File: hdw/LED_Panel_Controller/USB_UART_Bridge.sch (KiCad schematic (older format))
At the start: 37 parts, among them J1501 USB_B_Mini, U1501 TLV6700, U1502 FT234XD, U1503 TXB0102DCU, U1504 TPD3S014DBVR

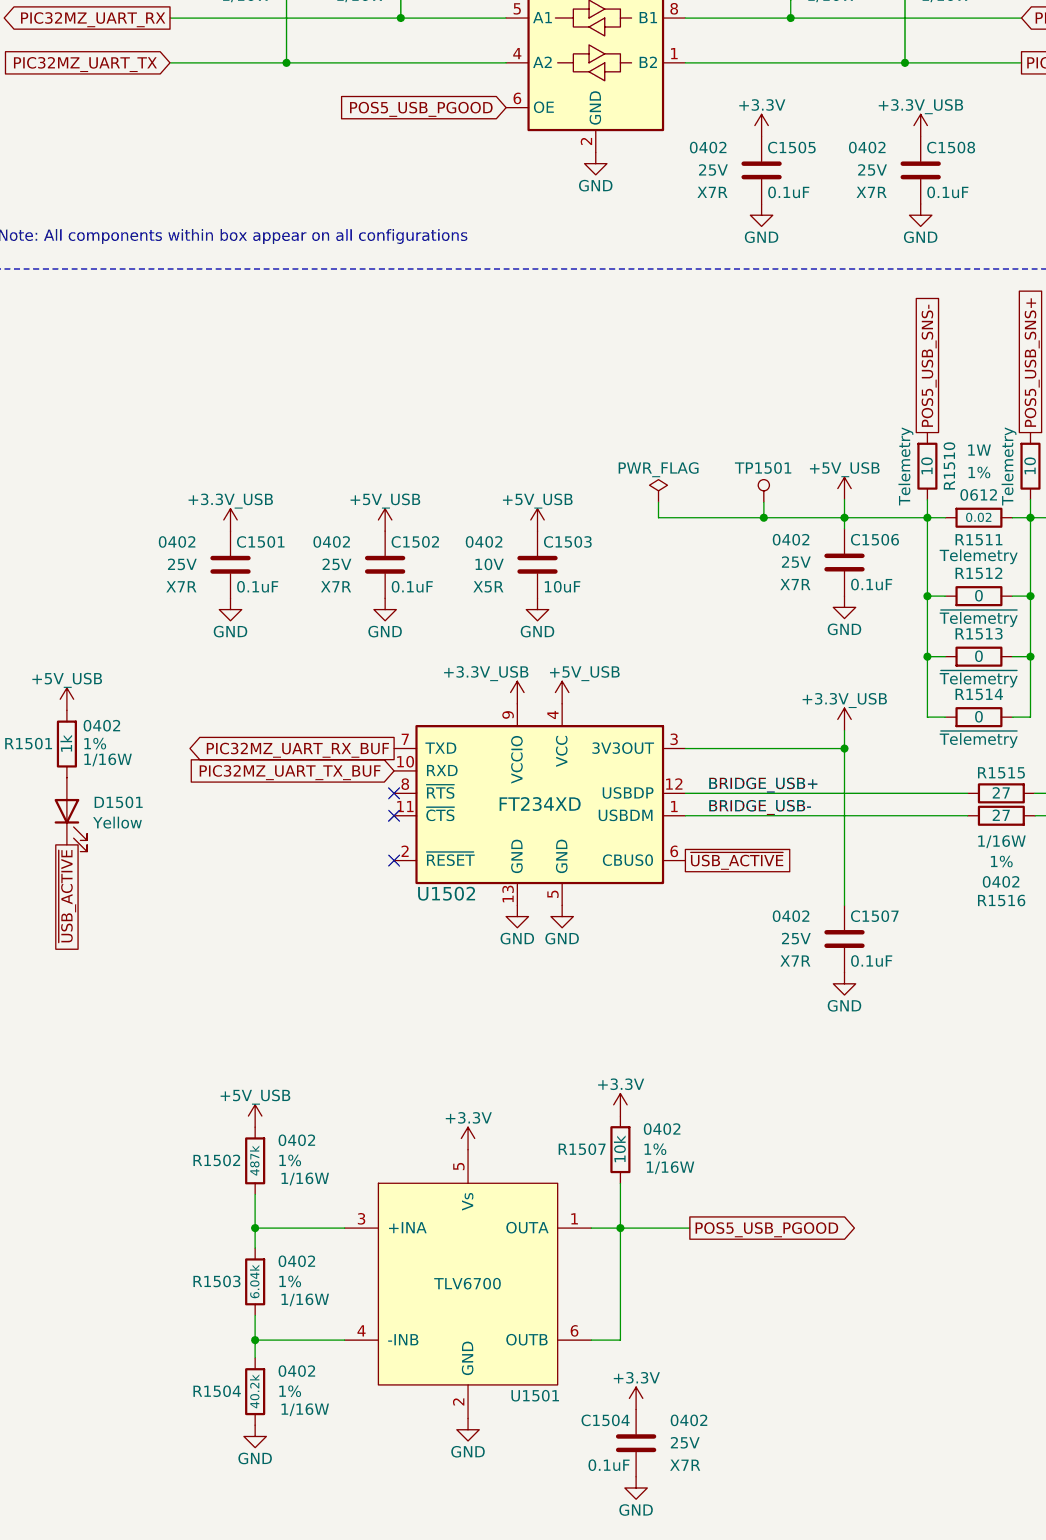
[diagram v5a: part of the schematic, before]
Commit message: added BOMs, some consolidation
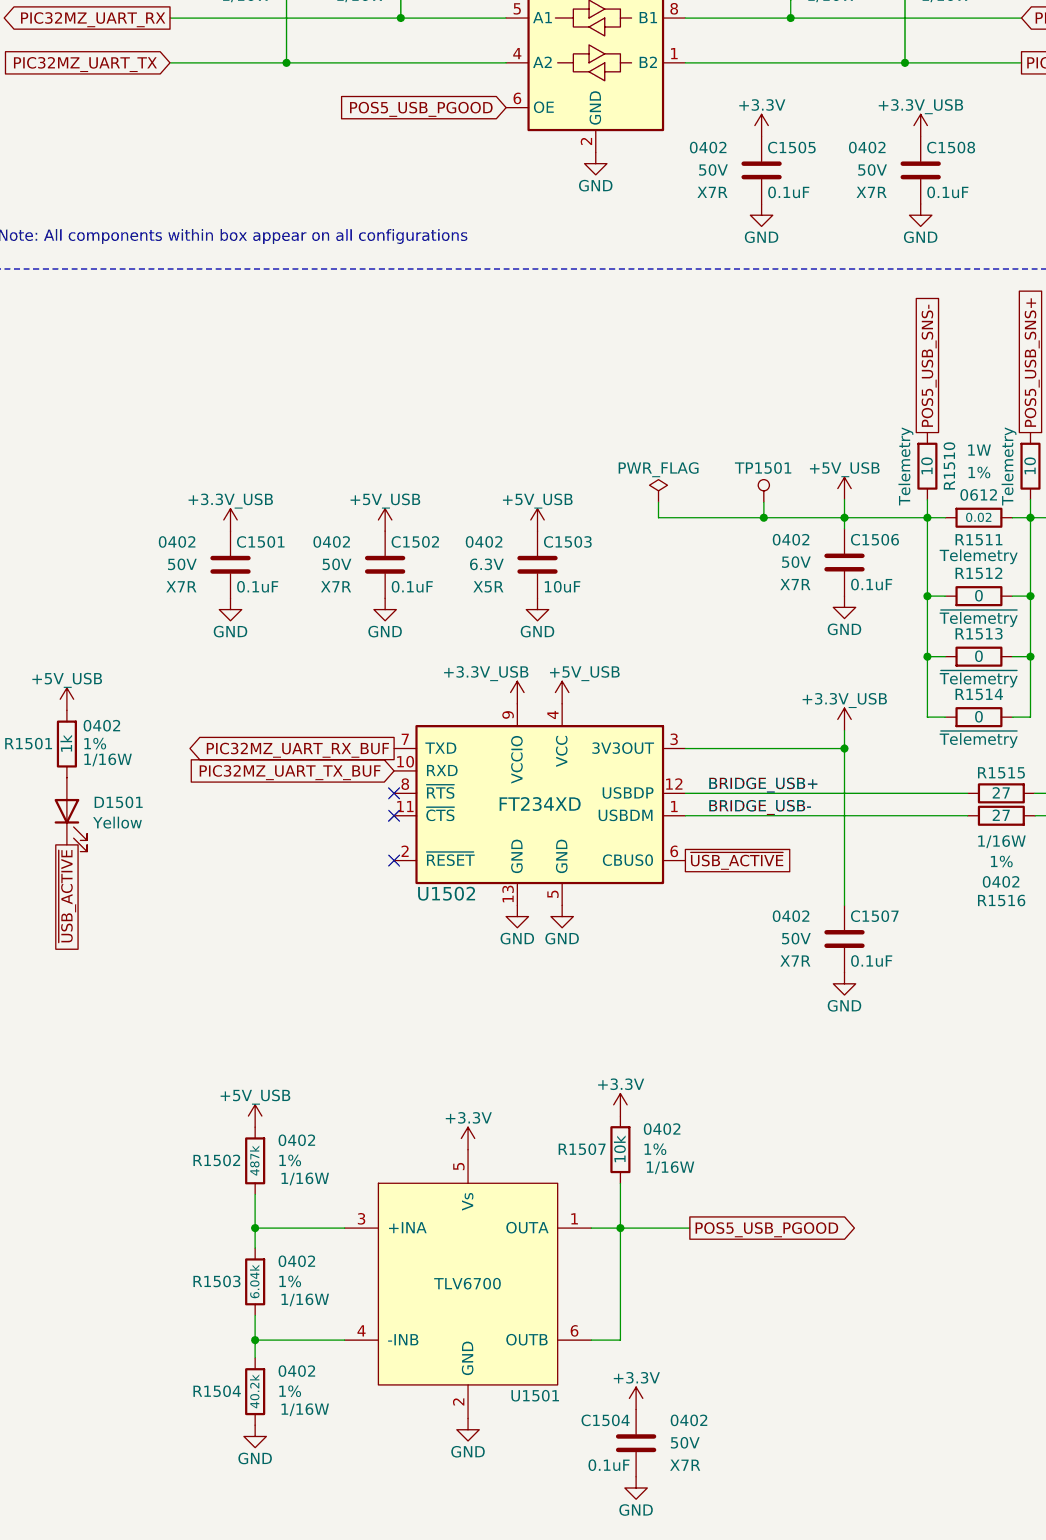
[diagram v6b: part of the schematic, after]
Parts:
- C1203: Digi-Key PN 1276-6830-1-ND -> 1276-1451-1-ND; Voltage 10V -> 6.3V
- C1204, C1501, C1502, C1505, C1506, C1507, C1508: Voltage 25V -> 50V
- R1210, R1211, R1212: Digi-Key PN 2019-RK73Z1ETTPCT-ND -> RMCF0402ZT0R00CT-N
- R1504: Digi-Key PN 311-40.2KLRCT-ND -> RMCF0402FT40K2CT-ND
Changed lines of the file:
@@
 F 3 "" H 2385 3780 50  0001 C CNN
 F 4 "0402" H 2210 3780 50  0000 R CNN "display_footprint"
-F 5 "25V" H 2210 3680 50  0000 R CNN "Voltage"
+F 5 "50V" H 2210 3680 50  0000 R CNN "Voltage"
 F 6 "X7R" H 2210 3580 50  0000 R CNN "Dielectric"
 F 7 "490-10698-1-ND" H 2785 4180 60  0001 C CNN "Digi-Key PN"
@@
 F 3 "" H 1695 3780 50  0001 C CNN
 F 4 "0402" H 1520 3780 50  0000 R CNN "display_footprint"
-F 5 "25V" H 1520 3680 50  0000 R CNN "Voltage"
+F 5 "50V" H 1520 3680 50  0000 R CNN "Voltage"
 F 6 "X7R" H 1520 3580 50  0000 R CNN "Dielectric"
 F 7 "490-10698-1-ND" H 2095 4180 60  0001 C CNN "Digi-Key PN"
@@
 F 3 "" H 4435 5450 50  0001 C CNN
 F 4 "0402" H 4260 5450 50  0000 R CNN "display_footprint"
-F 5 "25V" H 4260 5350 50  0000 R CNN "Voltage"
+F 5 "50V" H 4260 5350 50  0000 R CNN "Voltage"
 F 6 "X7R" H 4260 5250 50  0000 R CNN "Dielectric"
 F 7 "490-10698-1-ND" H 4835 5850 60  0001 C CNN "Digi-Key PN"
@@
 F 5 "1%" H 1880 7370 50  0000 L CNN "Tolerance"
 F 6 "1/16W" H 1890 7290 50  0000 L CNN "Wattage"
-F 7 "311-40.2KLRCT-ND" H 2080 7770 60  0001 C CNN "Digi-Key PN"
+F 7 "RMCF0402FT40K2CT-ND" H 2080 7770 60  0001 C CNN "Digi-Key PN"
 F 8 "USB" H 1780 7370 50  0001 C CNN "Configuration"
 	1    1780 7370
@@
 F 4 "490-10698-1-ND" H 3905 8100 60  0001 C CNN "Digi-Key PN"
 F 5 "0402" H 3330 7700 50  0000 R CNN "display_footprint"
-F 6 "25V" H 3330 7600 50  0000 R CNN "Voltage"
+F 6 "50V" H 3330 7600 50  0000 R CNN "Voltage"
 F 7 "X7R" H 3330 7500 50  0000 R CNN "Dielectric"
 F 8 "USB" H 3480 7600 50  0001 C CNN "Configuration"
@@
 F 3 "" H 4435 3770 50  0001 C CNN
 F 4 "0402" H 4260 3770 50  0000 R CNN "display_footprint"
-F 5 "25V" H 4260 3670 50  0000 R CNN "Voltage"
+F 5 "50V" H 4260 3670 50  0000 R CNN "Voltage"
 F 6 "X7R" H 4260 3570 50  0000 R CNN "Dielectric"
 F 7 "490-10698-1-ND" H 4835 4170 60  0001 C CNN "Digi-Key PN"
@@
 F 3 "" H 4065 2020 50  0001 C CNN
 F 4 "0402" H 3890 2020 50  0000 R CNN "display_footprint"
-F 5 "25V" H 3890 1920 50  0000 R CNN "Voltage"
+F 5 "50V" H 3890 1920 50  0000 R CNN "Voltage"
 F 6 "X7R" H 3890 1820 50  0000 R CNN "Dielectric"
 F 7 "490-10698-1-ND" H 4040 1920 50  0001 C CNN "Digi-Key PN"
@@
 F 3 "" H 4775 2020 50  0001 C CNN
 F 4 "0402" H 4600 2020 50  0000 R CNN "display_footprint"
-F 5 "25V" H 4600 1920 50  0000 R CNN "Voltage"
+F 5 "50V" H 4600 1920 50  0000 R CNN "Voltage"
 F 6 "X7R" H 4600 1820 50  0000 R CNN "Dielectric"
 F 7 "490-10698-1-ND" H 4750 1920 50  0001 C CNN "Digi-Key PN"
@@
 F 3 "" H 3065 3780 50  0001 C CNN
 F 4 "0402" H 2890 3780 50  0000 R CNN "display_footprint"
-F 5 "10V" H 2890 3680 50  0000 R CNN "Voltage"
+F 5 "6.3V" H 2890 3680 50  0000 R CNN "Voltage"
 F 6 "X5R" H 2890 3580 50  0000 R CNN "Dielectric"
-F 7 "1276-6830-1-ND" H 3040 3680 50  0001 C CNN "Digi-Key PN"
+F 7 "1276-1451-1-ND" H 3040 3680 50  0001 C CNN "Digi-Key PN"
 F 8 "USB" H 3040 3680 50  0001 C CNN "Configuration"
 	1    3040 3680
@@
 F 6 "1/16W" V 5310 3820 50  0001 C CNN "Wattage"
 F 7 "~Telemetry" V 5110 3820 50  0000 C CNN "Configuration"
-F 8 "2019-RK73Z1ETTPCT-ND" H 5010 3820 50  0001 C CNN "Digi-Key PN"
+F 8 "RMCF0402ZT0R00CT-N" H 5010 3820 50  0001 C CNN "Digi-Key PN"
 	1    5010 3820
 	0    -1   1    0
@@
 F 6 "1/16W" V 5310 4090 50  0001 C CNN "Wattage"
 F 7 "~Telemetry" V 5110 4090 50  0000 C CNN "Configuration"
-F 8 "2019-RK73Z1ETTPCT-ND" H 5010 4090 50  0001 C CNN "Digi-Key PN"
+F 8 "RMCF0402ZT0R00CT-N" H 5010 4090 50  0001 C CNN "Digi-Key PN"
 	1    5010 4090
 	0    -1   1    0
@@
 F 6 "1/16W" V 5310 4360 50  0001 C CNN "Wattage"
 F 7 "~Telemetry" V 5110 4360 50  0000 C CNN "Configuration"
-F 8 "2019-RK73Z1ETTPCT-ND" H 5010 4360 50  0001 C CNN "Digi-Key PN"
+F 8 "RMCF0402ZT0R00CT-N" H 5010 4360 50  0001 C CNN "Digi-Key PN"
 	1    5010 4360
 	0    -1   1    0
